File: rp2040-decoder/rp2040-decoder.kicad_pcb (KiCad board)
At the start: 4 copper layers, 19.6 x 8.6 mm, 51 parts, among them J4 5050662422, Q1 TPM2008, Q2 TPM2008, Q3 TPM2008, Q5 TPM2008, Q6 TPM2008, SW1 BOOT, U1 W25Q16JVUXIQ, U2 MT2492, U3 RP2040, U4 MD9927, U5 MAX98357A, Y1 X252012MMB4SI

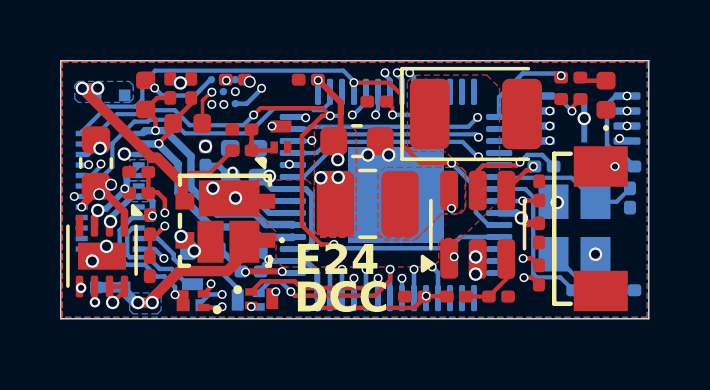
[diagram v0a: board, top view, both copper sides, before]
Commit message: feat: upgrade flash to 8MB
feat: reorganize layout to be cleaner
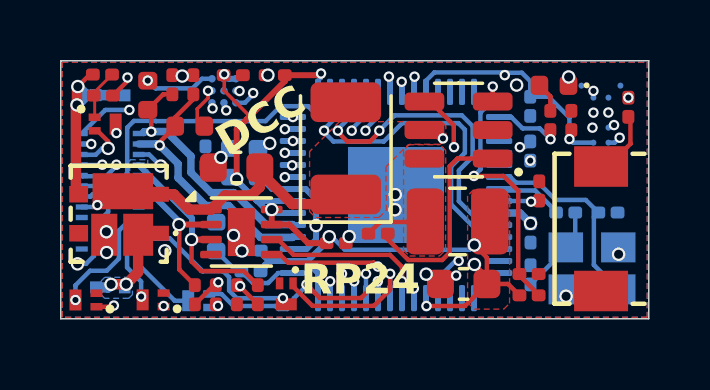
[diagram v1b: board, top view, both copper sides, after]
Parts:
- C17, C7, Q5: moved to B.Cu
- J4: value 5050662422 -> 5052702412
- Q2, Q6, R4: moved to F.Cu
- U1: value W25Q16JVUXIQ -> W25Q64JWBYIQ; footprint Package_SON:Winbond_USON-8-1EP_3x2mm_P0.5mm_EP0.2x1.6mm -> Local Library:Winbond_WLCSP-12_P0.5mm
- moved C9 5.94 mm to (113.4, 107.2), turned to 180 degrees
- moved Q1 5.88 mm to (101.4, 101.9), turned to 0 degrees
- moved C6 5.53 mm to (110.5, 105.6), turned to 180 degrees
- moved R1 5.29 mm to (101.3, 100.3)
- moved R14 5.24 mm to (105.8, 107.6), turned to 90 degrees
- moved R13 5.22 mm to (106.5, 107.6), turned to 90 degrees
- moved C17 5.11 mm to (115.6, 101.3), turned to -90 degrees
- moved R2 4.76 mm to (101.4, 101.0), turned to 180 degrees
- moved U4 4.71 mm to (106.0, 105.5), turned to 0 degrees
- moved C18 4.69 mm to (105.8, 103.4), turned to 180 degrees
- moved C4 4.49 mm to (109.5, 102.7), turned to 90 degrees
- moved Q3 3.57 mm to (100.8, 107.8)
- moved D1 3.55 mm to (101.9, 104.9)
- moved U2 3.22 mm to (113.2, 102.1), turned to 180 degrees
- moved C3 3.18 mm to (115.6, 106.9), turned to 90 degrees
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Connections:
- U3 pad 51: Net-(U1-IO3) -> Net-(U1-IO2)
- U3 pad 52: Net-(U1-CLK) -> Net-(U1-IO3)
- U3 pad 53: Net-(U1-DI(IO0)) -> Net-(U1-CLK)
- U3 pad 54: Net-(U1-IO2) -> Net-(U1-DO(IO1))
- U3 pad 55: Net-(U1-DO(IO1)) -> Net-(U1-DI(IO0))
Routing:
- net +3.3V: track 28.8 -> 46.3 mm, vias 14 -> 12
- net /GPIO23: track 15.0 -> 5.76 mm, vias 2 -> 1
- net /GPIO22: track 15.1 -> 5.98 mm
- net Net-(U2-FB): track 2.44 -> 9.22 mm, vias 0 -> 2
- net VDC: track 6.58 -> 13.1 mm, vias 6 -> 3
- net /GPIO21: track 11.0 -> 15.5 mm
- net /ADC_EMF_B: track 9.43 -> 5.56 mm
- net Net-(U1-DI(IO0)): track 8.97 -> 12.6 mm
- net /MOTOR_B: track 3.57 -> 7.14 mm, vias 2 -> 1
- net Net-(U2-EN): track 1.27 -> 4.66 mm, vias 1 -> 2
- net Net-(U2-BS): track 3.77 -> 7.06 mm, vias 2 -> 0
- net /GPIO26: track 7.46 -> 10.7 mm
- net /TRACK_RIGHT: track 6.41 -> 3.13 mm
- net Net-(U3-XOUT): track 5.37 -> 2.25 mm
- net GND: track 2.52 -> 5.64 mm, vias 21 -> 23
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- removed copper zone on B.Cu, net /TRACK_LEFT
- removed copper zone on In2.Cu, net VDC
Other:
- board text added: "RP24"
- board text removed: "E24"

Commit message: feat: add external capacitor support
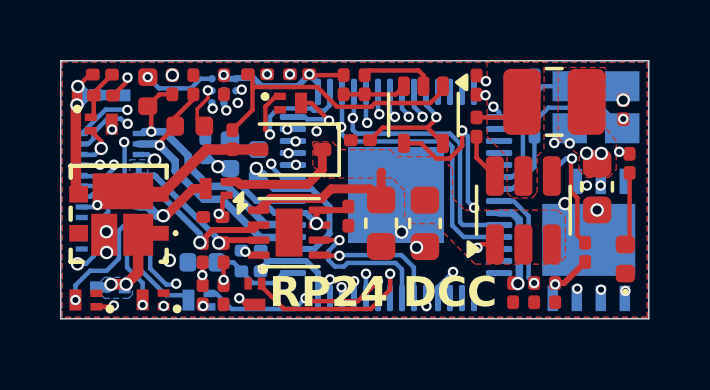
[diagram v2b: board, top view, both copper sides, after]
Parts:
- removed R5: 100k, Resistor_SMD:R_0201_0603Metric
- removed R7: 22k, Resistor_SMD:R_0201_0603Metric
- removed R8: 49.9k, Resistor_SMD:R_0201_0603Metric
- removed SW1: BOOT, Local Library:Xunpu_TS-1088-AR02016
- added C15: 10pF, Capacitor_SMD:C_0201_0603Metric, F.Cu at (105.0, 105.0)
- added C5: 100nF, Capacitor_SMD:C_0201_0603Metric, F.Cu at (109.9, 102.5)
- added D4: 1N5819WS, Diode_SMD:D_SOD-323, F.Cu at (107.6, 102.8)
- added Q4: TPM2008, Local Library:Diodes_DFN1006-3, F.Cu at (107.6, 101.2)
- added Q7: TPM2008, Local Library:Diodes_DFN1006-3, F.Cu at (105.1, 104.1)
- added R15: 1K, Resistor_SMD:R_0201_0603Metric, F.Cu at (117.4, 106.2)
- added R16: 20K, Resistor_SMD:R_0201_0603Metric, F.Cu at (109.4, 100.6)
- added R17: 33K, Resistor_SMD:R_0201_0603Metric, F.Cu at (110.1, 100.6)
- added R3: 100K, Resistor_SMD:R_0201_0603Metric, F.Cu at (105.7, 102.4)
- added U6: LMV331, Package_TO_SOT_SMD:SOT-353_SC-70-5, F.Cu at (112.0, 101.6)
- C17, C3, C7: moved to F.Cu
- C4: value 22uF -> 10uF; footprint Capacitor_Tantalum_SMD:CP_EIA-3528-21_Kemet-B -> Capacitor_SMD:C_0603_1608Metric
- C6: value 22nF -> 100nF
- L1: value 10uH -> 4.7uH
- R1, R11, R13, R2: value 6.8k -> 6.8K
- R12, R14, R6, R9: value 1k -> 1K
- R4: value 1k -> 33K
- U1: value W25Q64JWBYIQ -> W25Q64JVXGIQ; footprint Local Library:Winbond_WLCSP-12_P0.5mm -> Local Library:W25Q64JVXGIQ
- U2: value MT2492 -> AP63203WU; footprint Package_TO_SOT_SMD:SOT-23-6 -> Package_TO_SOT_SMD:TSOT-23-6
- moved R4 12.4 mm to (106.5, 100.2), turned to 0 degrees
- moved C3 6.31 mm to (118.7, 101.4)
- moved D2 6.26 mm to (118.8, 106.4), turned to 90 degrees
- moved C2 5.77 mm to (116.4, 107.5), turned to -90 degrees
- moved C9 5.50 mm to (117.8, 104.0), turned to -90 degrees
- moved Y1 5.37 mm to (117.8, 101.3), turned to 180 degrees
- moved C18 5.16 mm to (110.6, 105.2), turned to -90 degrees
- moved L1 5.13 mm to (116.4, 101.2)
- moved C1 4.91 mm to (115.7, 100.6), turned to 90 degrees
- moved C6 4.83 mm to (113.8, 102.0), turned to 90 degrees
- moved U1 4.01 mm to (117.5, 105.8), turned to -90 degrees
- moved C4 3.64 mm to (112.1, 105.2), turned to -90 degrees
- moved U2 3.43 mm to (115.4, 104.8), turned to 90 degrees
- moved C13 3.39 mm to (115.7, 107.5), turned to -90 degrees
- moved R6 3.03 mm to (115.7, 102.0), turned to 90 degrees
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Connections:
- C18 pad 1: VDC -> /CAP_VDC
- C4 pad 1: VDC -> /CAP_VDC
- C6 pad 1: Net-(U2-BS) -> Net-(U2-BST)
- R4 pad 1: Net-(U1-~{CS}) -> /COMP_P
- R4 pad 2: Net-(R4-Pad2) -> GND
- U2 pad 1: Net-(U2-BS) -> +3.3V
- U2 pad 2: GND -> /CAP_VDC
- U2 pad 3: Net-(U2-FB) -> /CAP_VDC
- U2 pad 4: Net-(U2-EN) -> GND
- U2 pad 5: VDC -> /SWITCH
- U2 pad 6: /SWITCH -> Net-(U2-BST)
- U3 pad 56: Net-(U1-~{CS}) -> /BOOT
- U4 pad 1: VDC -> /CAP_VDC
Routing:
- net /BOOT: track 0.00 -> 15.4 mm, vias 0 -> 2
- net Net-(U1-~{CS}): track 15.2 -> 0.00 mm, vias 3 -> 0
- net /CAP_ENABLE: track 0.00 -> 15.1 mm, vias 0 -> 3
- net /CAP_VDC: track 0.00 -> 9.56 mm
- net Net-(U2-FB): track 9.22 -> 0.00 mm, vias 2 -> 0
- net /COMP_P: track 0.00 -> 9.19 mm
- net VDC: track 13.1 -> 4.68 mm, vias 3 -> 1
- net Net-(U2-BS): track 7.06 -> 0.00 mm
- net +1V1: track 13.3 -> 20.2 mm
- net Net-(U1-IO2): track 13.3 -> 19.1 mm
- net Net-(U2-EN): track 4.66 -> 0.00 mm, vias 2 -> 0
- net Net-(U1-DI(IO0)): track 12.6 -> 15.9 mm
- net Net-(U3-GPIO12): track 2.33 -> 5.62 mm, vias 1 -> 2
- net Net-(U1-DO(IO1)): track 13.5 -> 10.7 mm
- net /CAP+: track 0.00 -> 2.72 mm, vias 0 -> 1
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- added copper zone on F.Cu, net /CAP_VDC
- removed copper zone on F.Cu, net VDC
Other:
- board text added: "RP24 DCC"
- board text removed: "DCC"
- board text removed: "RP24"

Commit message: fix: dfm fixes and trace cleanup
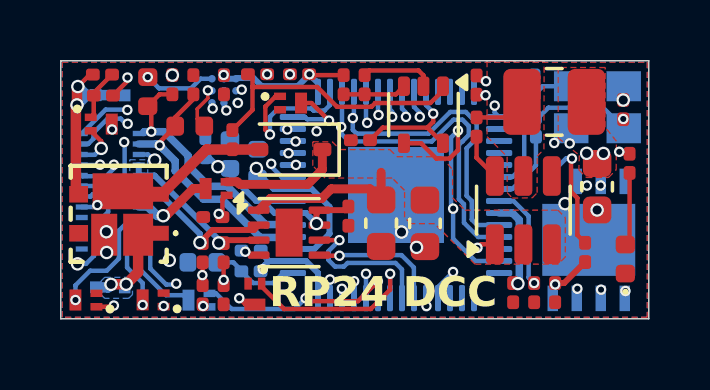
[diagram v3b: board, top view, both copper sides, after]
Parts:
- moved R6 0.05 mm to (115.8, 102.0)
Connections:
- U3 pad 27: unconnected-(U3-GPIO16-Pad27) -> /CAP_ENABLE
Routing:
- net /CAP_ENABLE: track 15.1 -> 17.2 mm
- net /AUX11: track 20.5 -> 21.8 mm
- net /AUX12: track 20.1 -> 21.4 mm
- net +3.3V: track 43.9 -> 42.6 mm
- net /SWITCH: track 1.73 -> 1.00 mm
- net /ADC_EMF_B: track 5.85 -> 5.34 mm

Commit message: fix: allow cap to discharge below 8V rail voltage
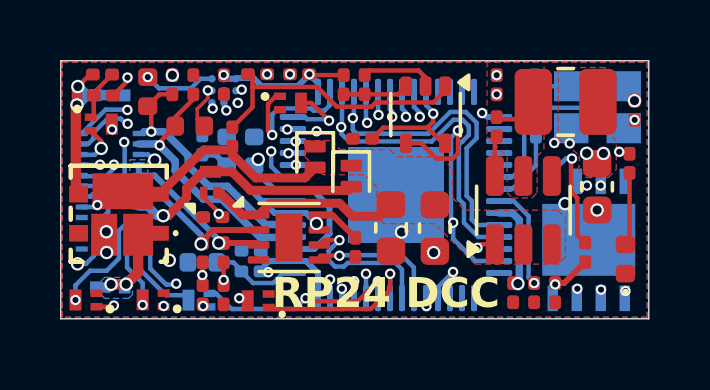
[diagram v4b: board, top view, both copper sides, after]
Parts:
- added D3: PSBD2FD40V1H, Diode_SMD:D_SOD-882, F.Cu at (109.6, 103.7)
- D4: value 1N5819WS -> PSBD2FD40V1H; footprint Diode_SMD:D_SOD-323 -> Diode_SMD:D_SOD-882
- moved C19 1.07 mm to (109.8, 106.0)
- moved D4 0.85 mm to (108.4, 103.0), turned to -90 degrees
- moved C17 0.67 mm to (114.5, 100.6)
- moved C6 0.67 mm to (114.5, 102.0)
- moved C8 0.42 mm to (106.4, 102.8)
- moved C3 0.38 mm to (119.1, 101.5)
- moved L1 0.38 mm to (116.8, 101.2)
- moved C4 0.37 mm to (112.4, 105.4)
- moved C18 0.36 mm to (111.0, 105.4)
- moved Q7 0.28 mm to (104.9, 103.8), turned to 90 degrees
- moved Q2 0.25 mm to (106.5, 107.8), turned to 180 degrees
- moved U4 0.16 mm to (107.6, 105.7)
- moved C10 0.14 mm to (105.5, 102.8)
- moved C12 0.13 mm to (104.7, 102.6)
- moved R3 0.09 mm to (105.7, 102.3)
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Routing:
- net /CAP+: track 2.72 -> 8.30 mm
- net /CAP_VDC: track 9.55 -> 6.60 mm
- net VDC: track 4.41 -> 7.10 mm
- net +3.3V: track 42.6 -> 43.8 mm, vias 14 -> 13
- net Net-(U3-GPIO12): track 5.71 -> 6.47 mm
- net Net-(U1-IO2): track 19.0 -> 19.7 mm
- net /GPIO24: track 6.20 -> 5.68 mm
- net GND: track 5.94 -> 5.73 mm, vias 21 -> 20

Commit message: fix: update footprints and component rotations
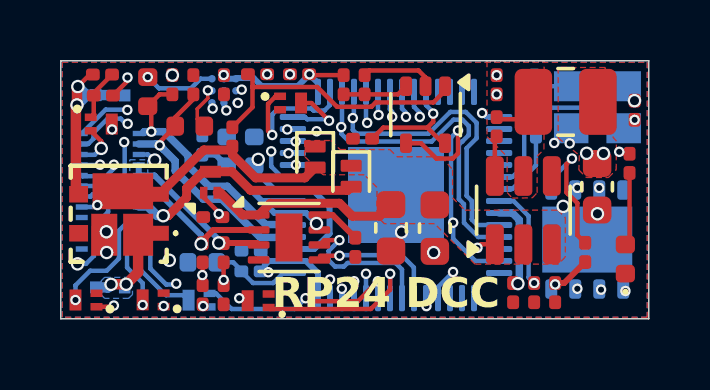
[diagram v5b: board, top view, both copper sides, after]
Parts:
- U1: footprint Local Library:W25Q64JVXGIQ -> Package_SON:WSON-8-1EP_4x4mm_P0.8mm_EP2.2x3mm
- moved U1 0.05 mm to (117.5, 105.8)
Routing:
- net /BOOT: track 15.1 -> 15.7 mm
- net Net-(U1-DO(IO1)): track 10.7 -> 10.1 mm

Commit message: fix: more dfm fixes
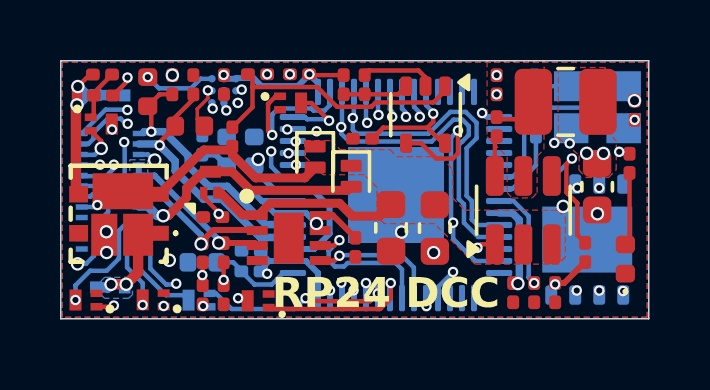
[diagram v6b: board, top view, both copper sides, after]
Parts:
- U4: footprint Package_DFN_QFN:DFN-8-1EP_2x2mm_P0.5mm_EP0.9x1.6mm -> Local Library:LM293QT
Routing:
- net /GPIO27: track 7.89 -> 7.28 mm
- net /GPIO25: track 6.86 -> 6.28 mm
- net /ADC_EMF_B: track 5.34 -> 5.88 mm

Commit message: feat: increase motor driver cap to 47uF
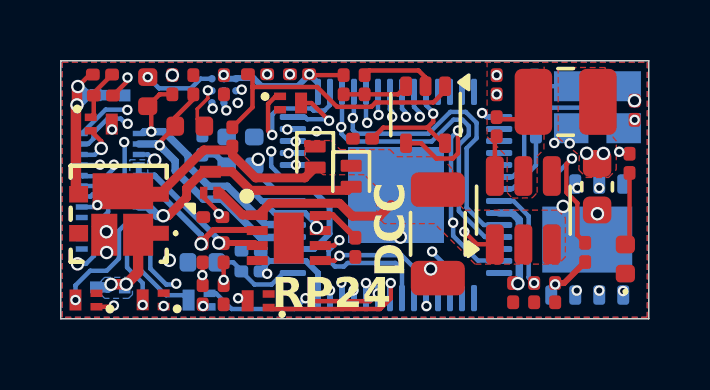
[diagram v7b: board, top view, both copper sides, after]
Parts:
- removed C4: 10uF, Capacitor_SMD:C_0603_1608Metric
- C18: value 10uF -> 47uF; footprint Capacitor_SMD:C_0603_1608Metric -> Capacitor_SMD:C_1206_3216Metric
- moved C18 1.57 mm to (112.5, 105.6)
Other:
- board text added: "DCC"
- board text added: "RP24"
- board text removed: "RP24 DCC"

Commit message: fix: shrink usb differential traces
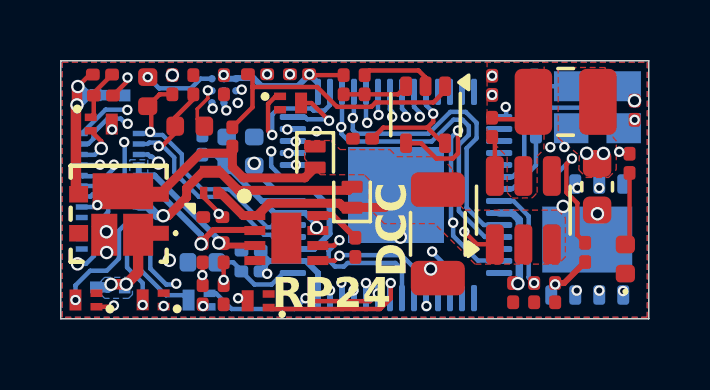
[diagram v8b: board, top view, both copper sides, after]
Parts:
- moved D3 0.70 mm to (109.7, 104.3), turned to 90 degrees
- moved C17 0.15 mm to (114.3, 100.6)
- moved C6 0.15 mm to (114.3, 102.0)
- moved U4 0.08 mm to (107.5, 105.7)
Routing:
- net Net-(U3-GPIO12): track 6.47 -> 5.12 mm
